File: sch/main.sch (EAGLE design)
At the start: 22 parts, among them IC2 PIC16F628P, K1 TF2--5V, K2 TF2--5V, T1 BC547, T2 BC547

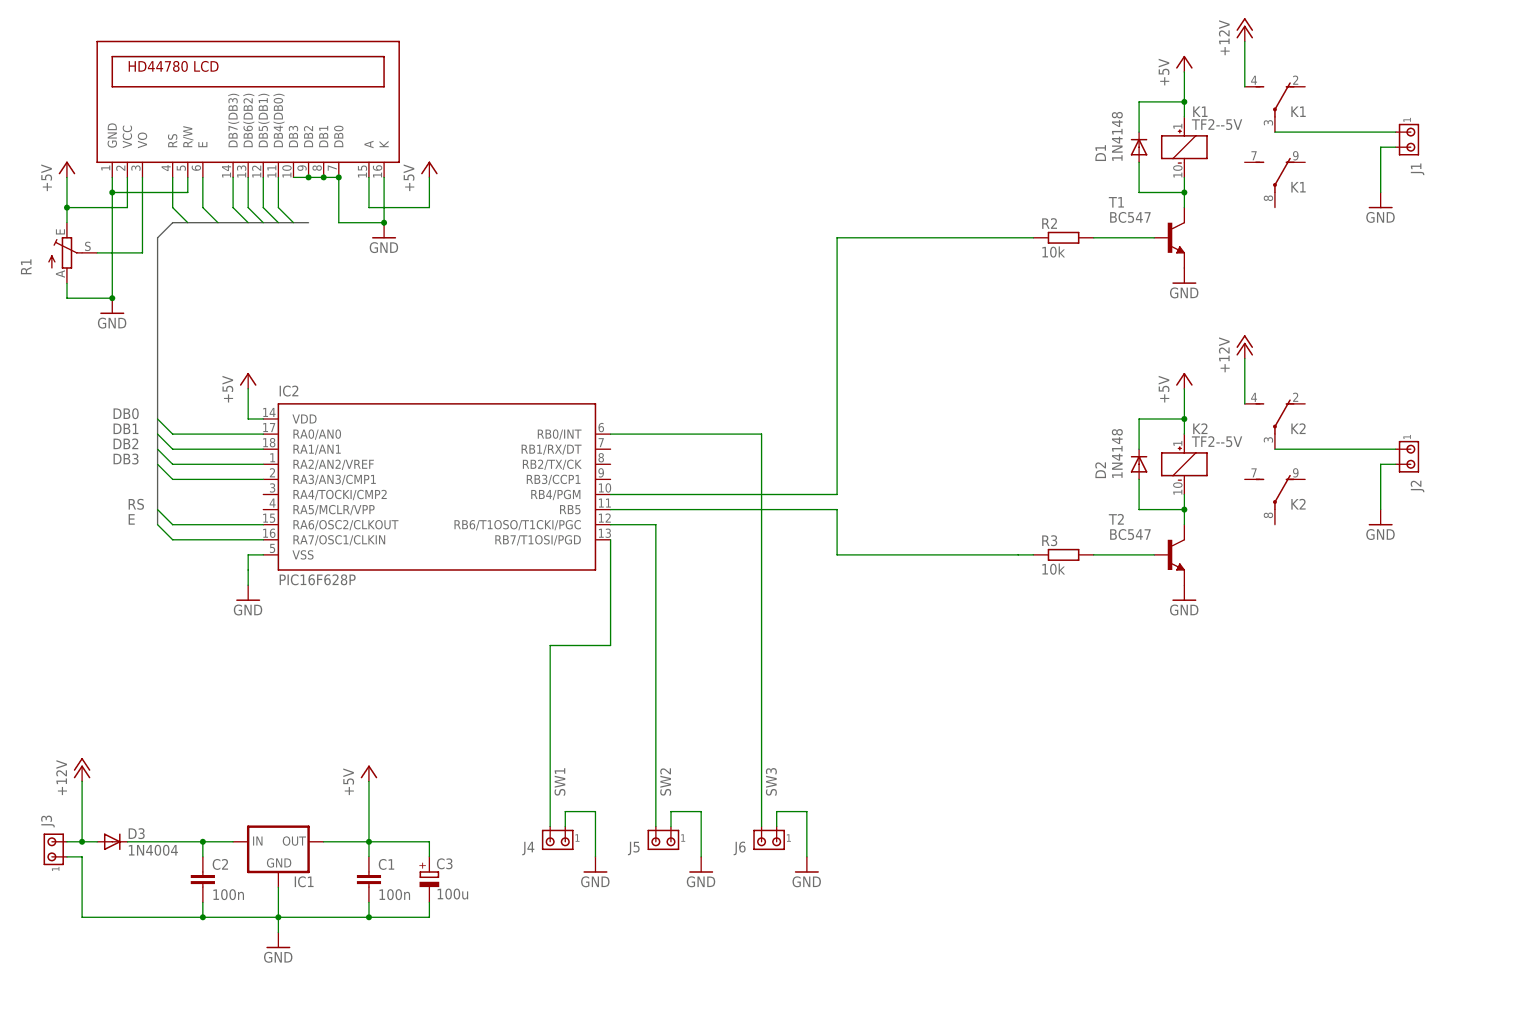
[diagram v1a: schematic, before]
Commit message: Replaced relays with transistors
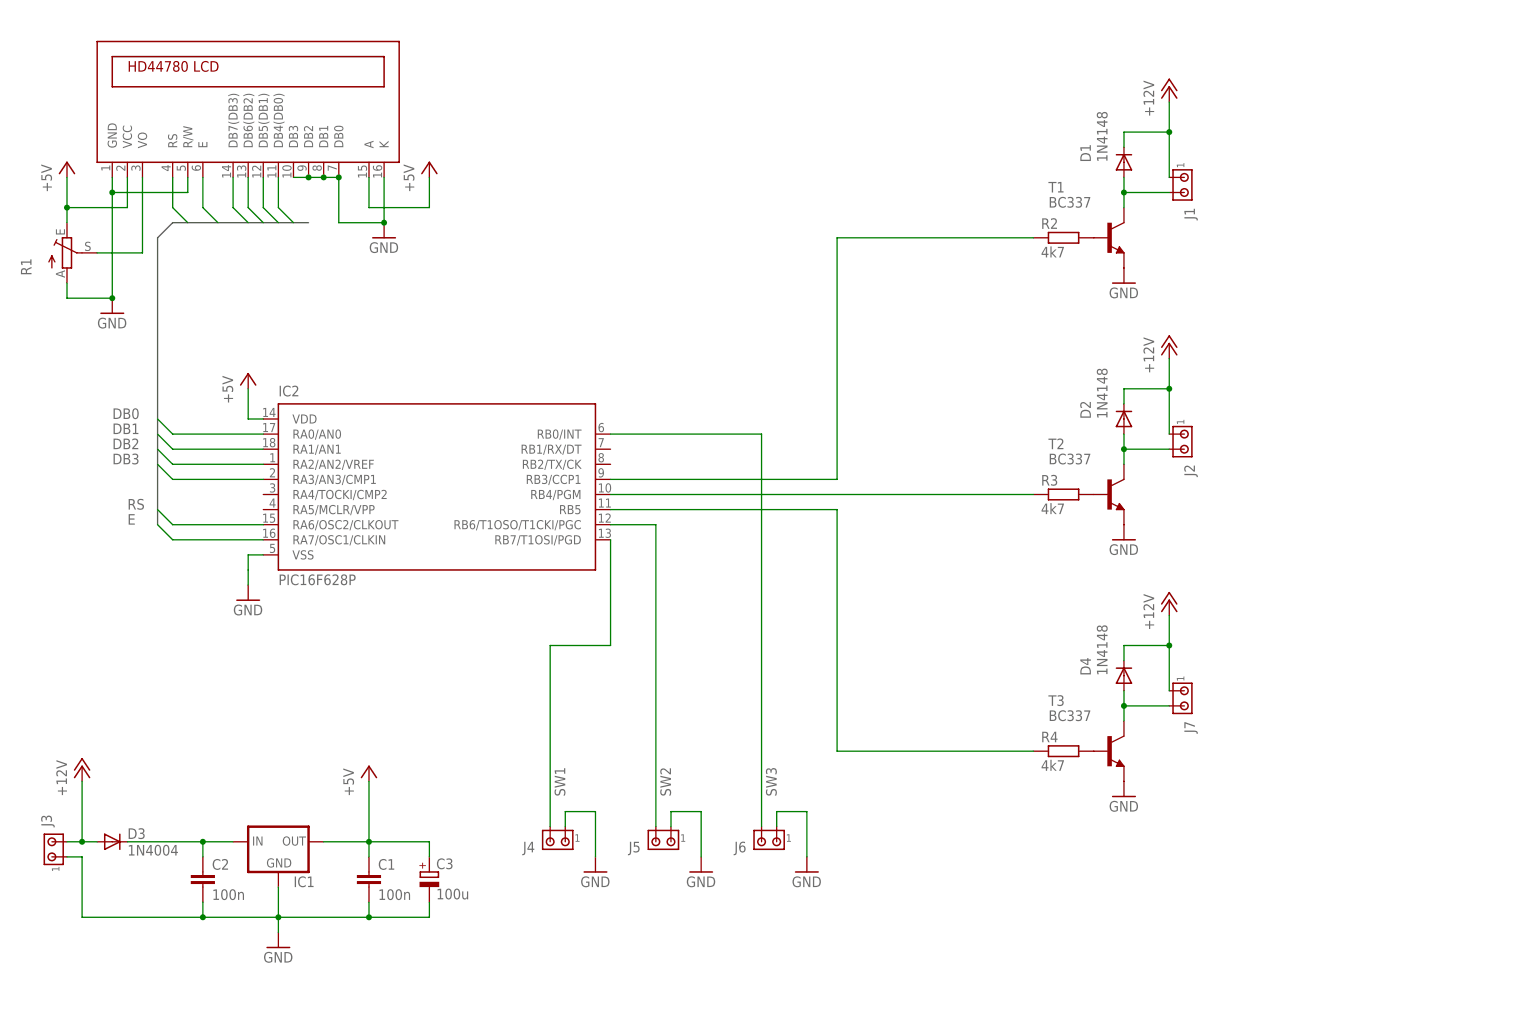
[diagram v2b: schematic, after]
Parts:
- removed K1, K2: TF2--5V, relay:TF2--5V
- added D4: 1N4148, diode:1N4148DO35-7
- added J7: (no value), con-amp:MTA02-100
- added R4: 4k7, rcl:R-EU_0207/10
- added T3: BC337, transistor:BC337-40-NPN-TO92-CBE
- R2, R3: value 10k -> 4k7
- T1, T2: value BC547 -> BC337; device transistor:BC547-NPN-TO92-CBE -> transistor:BC337-40-NPN-TO92-CBE
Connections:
- removed net N$1 (its old number): J1.1, K11.P
- removed net N$4 (its old number): D1.A, K1-.-, T1.C
- new net N$10: IC2.RB4/PGM, R3.1
- new net N$8: R4.2, T3.B
- new net N$9: D4.A, J7.2, T3.C
- net +12V: now also D1.C, D2.C, D4.C, J1.1, J2.1, J7.1; no longer K11.S, K21.S
- net +5V: no longer D1.C, D2.C, K1-.+, K2-.+
- net GND: now also T3.E; no longer J1.2, J2.2
- net N$2: now also D1.A, J1.2, T1.C; no longer J2.1, K21.P
- net N$5: now also J2.2; no longer K2-.-
- net N$6: now also IC2.RB3/CCP1; no longer IC2.RB4/PGM
- net N$7: now also R4.1; no longer R3.1
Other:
- moved on the sheet: D1, D2, J1, J2, R3, T1, T2

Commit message: First version for manufacturing
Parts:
- removed J1, J2, J3, J4, J5, J6, J7: (no value), con-amp:MTA02-100
- added S1, S2, S3: (no value), switch-omron:10-XX
- added S4: (no value), switch:320-916
- added U1: LCD_BL_16X2_LOW, lcdmodules2:LCD_BL_16X2_LOW
- added X1: D-SUB9-H2M09ST, con-thomas-betts:D-SUB9-H2M09ST
- U$1: value LCD_BL_16X2 -> KLDVX-0202-A; device lcdmodules:LCD_BL_16X2 -> con-kycon:KLDVX-0202-A
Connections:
- new net N$12: S4.P, U$1.1
- net +12V: now also S4.S, X1-1.F, X1-3.F, X1-5.F; no longer J1.1, J2.1, J3.2, J7.1
- net +5V: now also U1.A, U1.VCC; no longer U$1.A, U$1.VCC
- net DB0: now also U1.DB4(DB0); no longer U$1.DB4(DB0)
- net DB1: now also U1.DB5(DB1); no longer U$1.DB5(DB1)
- net DB2: now also U1.DB6(DB2); no longer U$1.DB6(DB2)
- net DB3: now also U1.DB7(DB3); no longer U$1.DB7(DB3)
- net E: now also U1.E; no longer U$1.E
- net GND: now also S1.P, S1.P1, S2.P, S2.P1, S3.P, S3.P1, U$1.2, U1.DB0, U1.DB1, U1.DB2, U1.DB3, U1.GND, U1.K, U1.R/W; no longer J3.1, J4.1, J5.1, J6.1, U$1.DB0, U$1.DB1, U$1.DB2, U$1.DB3, U$1.GND, U$1.K, U$1.R/W
- net N$11: now also U1.VO; no longer U$1.VO
- net N$2: now also X1-2.F; no longer J1.2
- net N$5: now also X1-4.F; no longer J2.2
- net N$9: now also X1-6.F; no longer J7.2
- net RS: now also U1.RS; no longer U$1.RS
- net SW1: now also S1.S, S1.S1; no longer J4.2
- net SW2: now also S2.S, S2.S1; no longer J5.2
- net SW3: now also S3.S, S3.S1; no longer J6.2
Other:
- moved on the sheet: C1, C2, C3, D3, IC1

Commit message: Updated 3d model
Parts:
- U1: value LCD_BL_16X2_LOW -> YM1602G_LOWCON
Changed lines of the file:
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@@
 <?xml version="1.0" encoding="utf-8"?>
 <!DOCTYPE eagle SYSTEM "eagle.dtd">
-<eagle version="6.2">
+<eagle version="6.1">
 <drawing>
 <settings>
@@
 <part name="U$1" library="con-kycon" deviceset="KLDVX-0202-" device="A"/>
 <part name="S4" library="switch" deviceset="320-916" device=""/>
-<part name="U1" library="lcdmodules2" deviceset="LCD_BL_16X2" device="_LOW"/>
+<part name="U1" library="lcdmodules2" deviceset="LCD_BL_16X2" device="_LOW" value="YM1602G_LOWCON"/>
 </parts>
 <sheets>

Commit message: Several packages change, re-routed
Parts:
- removed U$1: KLDVX-0202-A, con-kycon:KLDVX-0202-A
- added J1: (no value), con-jack:JACK-PLUG0
- added OK1, OK2, OK3: PC817, optocoupler:PC817
- added R10, R9: 10k, rcl:R-EU_0207/10
- added R5, R6, R8: 1k, rcl:R-EU_0207/10
- added R7: 3k3, rcl:R-EU_0207/10
- C1, C2: device rcl:C-EU050-025X075 -> rcl:C-EU025-025X050
- IC1: value (none) -> 7805; device v-reg:78XXS -> v-reg:78XXL
- R1: value (none) -> 4k7; device pot:TRIM_EU-CA9V -> pot:TRIM_EU-CA6V
- R2, R3: value 4k7 -> 3k3
- R4: value 4k7 -> 10k
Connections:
- new net N$13: OK1.A, R5.2
- new net N$14: OK1.EMIT, R2.1, R4.2
- new net N$15: OK2.EMIT, R10.2, R3.1
- new net N$16: OK3.A, R8.2
- new net N$17: R7.2, T2.B
- new net N$18: OK3.EMIT, R7.1, R9.2
- net +5V: now also OK1.COL, OK2.COL, OK3.COL
- net GND: now also J1.3, OK1.C, OK2.C, OK3.C, R10.1, R4.1, R9.1; no longer U$1.2
- net N$10: now also R8.1; no longer R3.1
- net N$12: now also J1.1; no longer U$1.1
- net N$4: now also OK2.A, R6.2; no longer R3.2, T2.B
- net N$6: now also R5.1; no longer R2.1
- net N$7: now also R6.1; no longer R4.1
- net N$8: now also R3.2; no longer R4.2
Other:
- moved on the sheet: D1, R2, R3, R4, T1

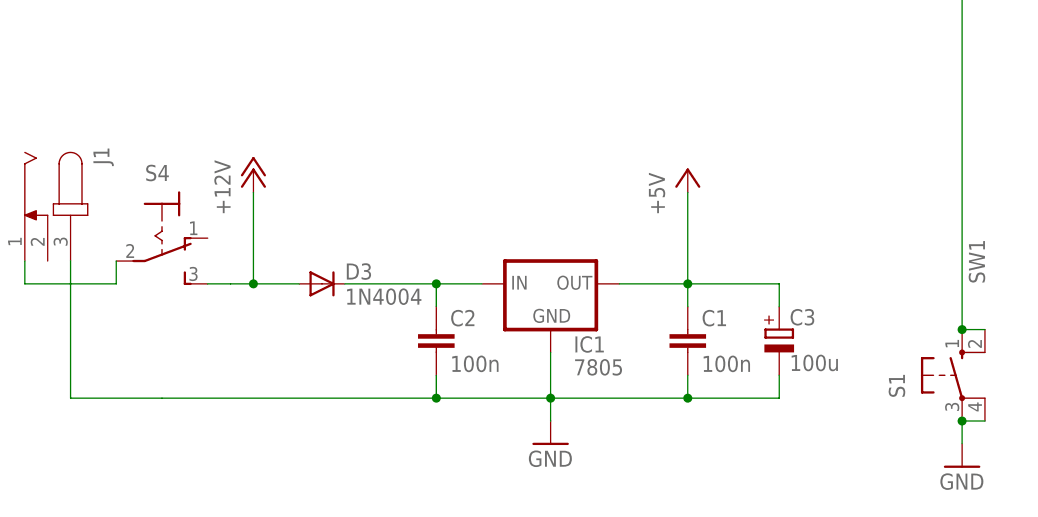
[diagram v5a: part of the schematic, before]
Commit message: Added capacitor to power input
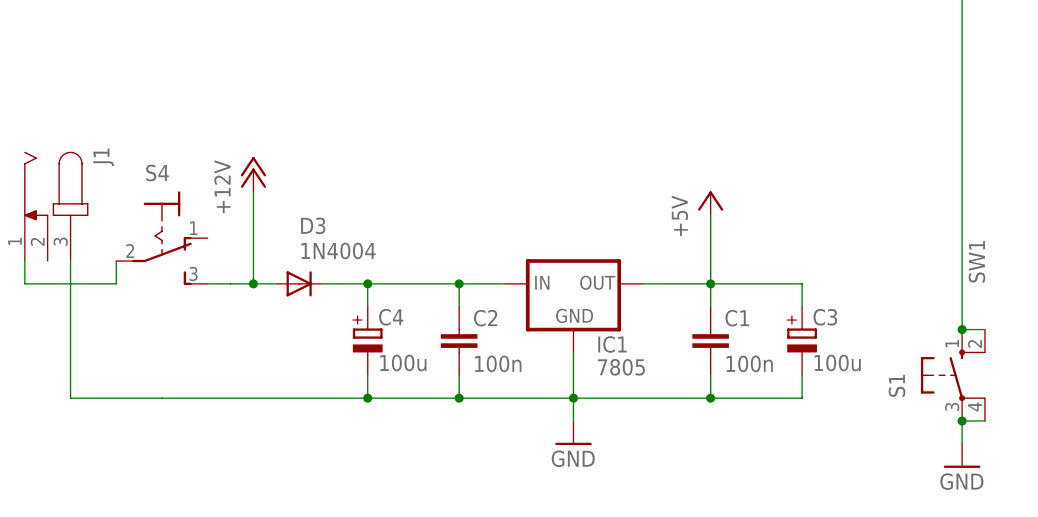
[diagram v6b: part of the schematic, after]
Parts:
- added C4: 100u, rcl:CPOL-EUE2.5-7
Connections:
- net GND: now also C4.-
- net N$3: now also C4.+
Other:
- moved on the sheet: C1, C2, C3, D3, IC1
